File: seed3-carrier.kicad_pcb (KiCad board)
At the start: 2 copper layers, 113 x 61.6 mm, 48 parts, among them J1 AudioJack2_Switch, J2 AudioJack2, J3 5V_IN, J4 DISPLAY_UART, J5 SJ1-3535NG, J6 Seed3_PINS_RIGHT, J7 Seed3_PINS_LEFT, Q1 AO3401A, U1 TLV9062IDR, U2 TPA6111A2DR

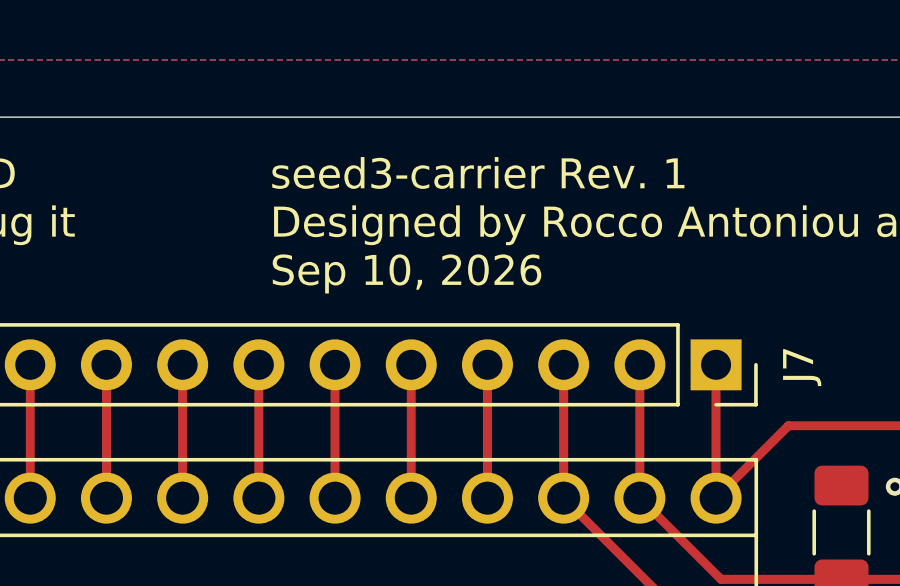
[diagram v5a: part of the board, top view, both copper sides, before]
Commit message: Simplify silkscreen revision date to Sep 2026
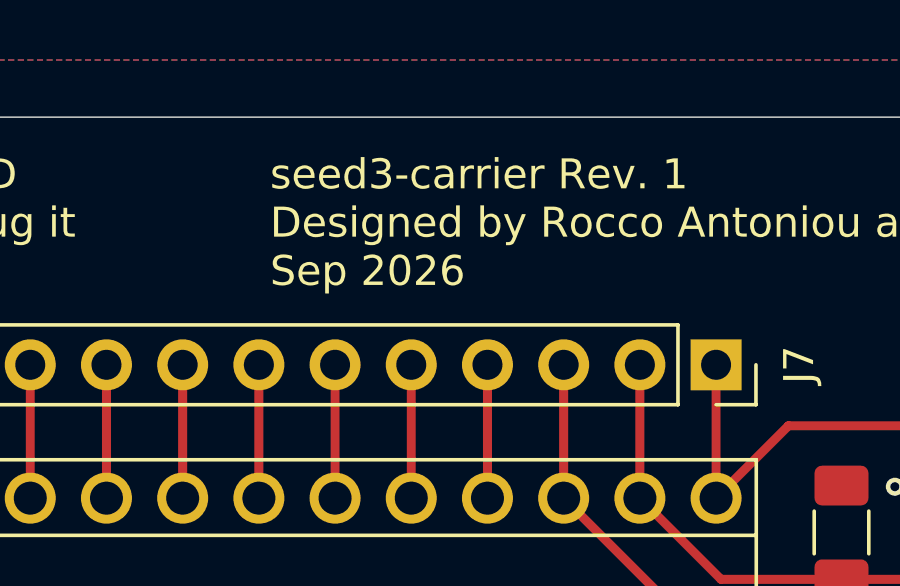
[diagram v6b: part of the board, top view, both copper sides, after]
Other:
- board text added: "seed3-carrier Rev. 1 Designed by Rocco Antoniou and Danny Diaz Reyes Sep 2026"
- board text removed: "seed3-carrier Rev. 1 Designed by Rocco Antoniou and Danny Diaz Reyes Sep 10, 2026"
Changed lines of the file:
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@@
 		)
 	)
-	(gr_text "seed3-carrier Rev. 1\nDesigned by Rocco Antoniou and Danny Diaz Reyes\nSep 10, 2026\n"
+	(gr_text "seed3-carrier Rev. 1\nDesigned by Rocco Antoniou and Danny Diaz Reyes\nSep 2026\n"
 		(at 86.106 45.72 0)
 		(layer "F.SilkS")

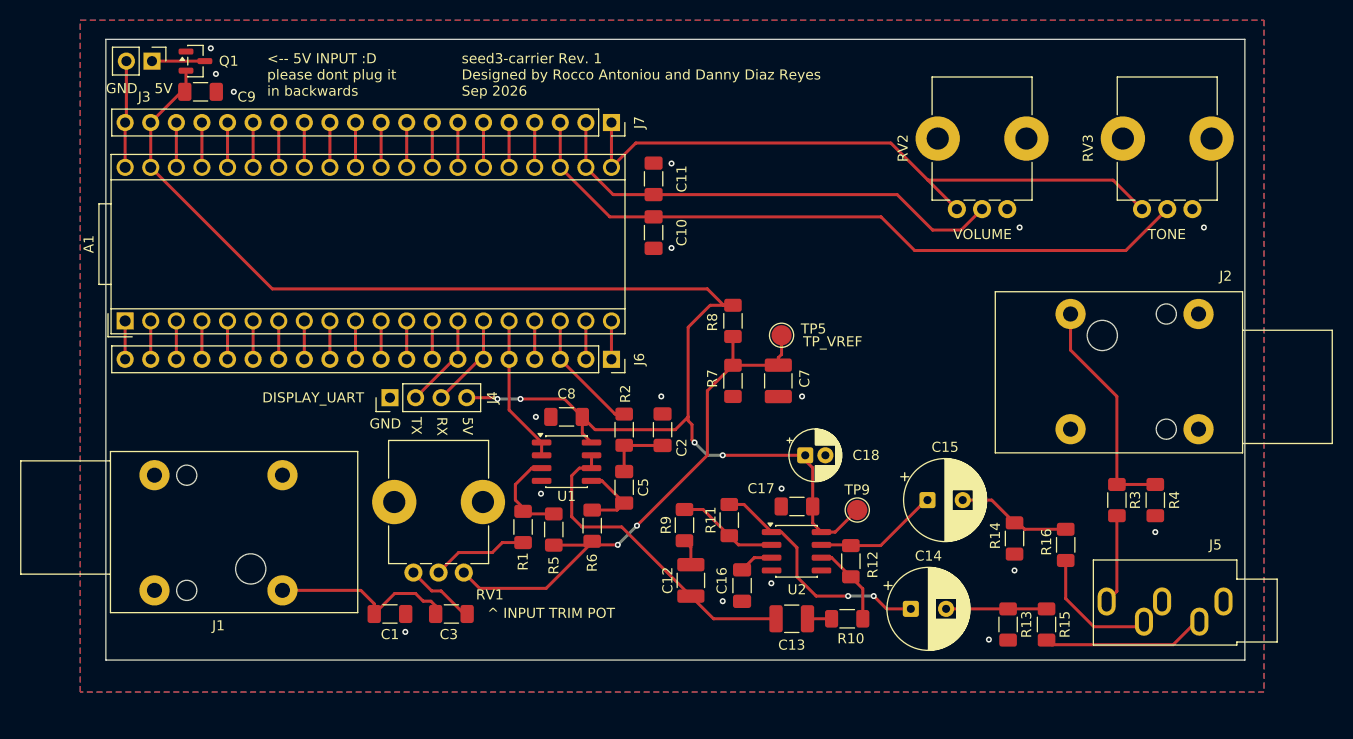
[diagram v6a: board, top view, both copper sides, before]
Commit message: Finalize potentiometer mounts and fabrication purchasing package
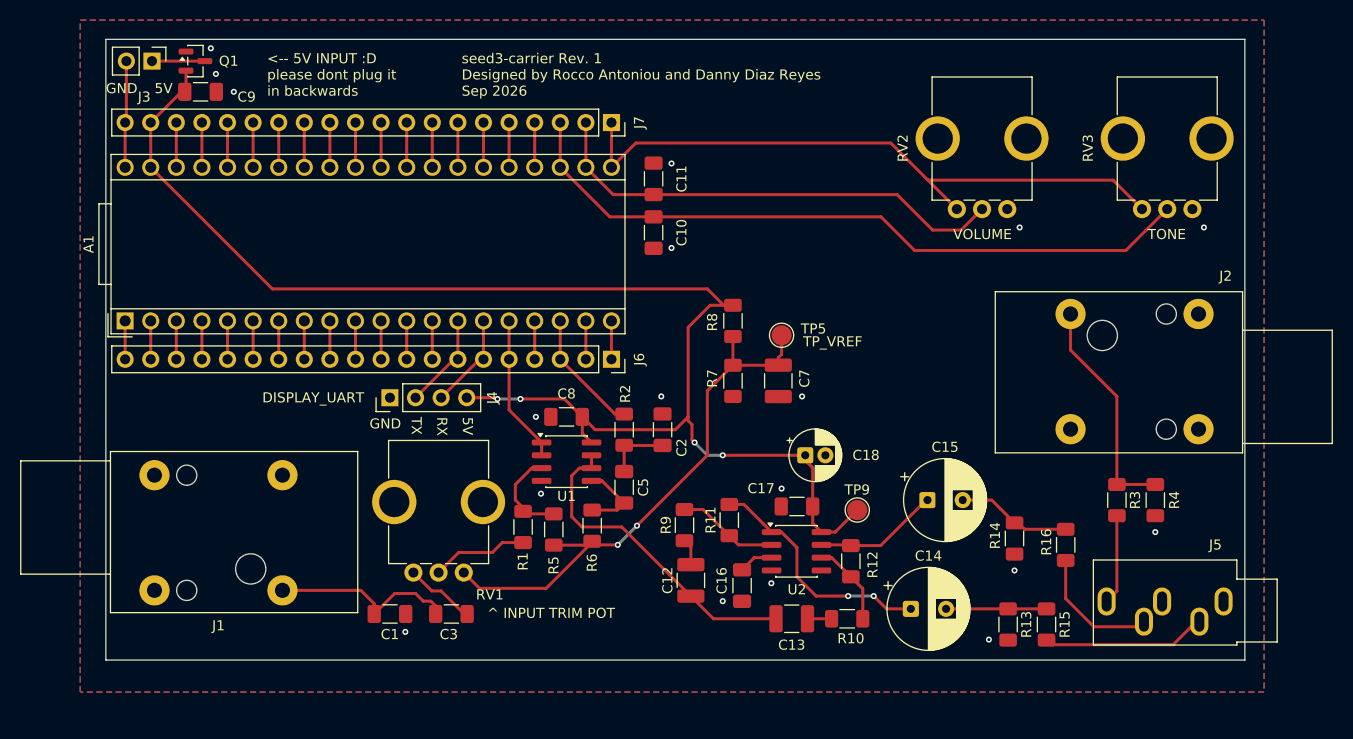
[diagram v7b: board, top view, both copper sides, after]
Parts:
- RV1, RV2, RV3: footprint Potentiometer_THT:Potentiometer_Bourns_PTV09A-1_Single_Vertical -> Seed3_Carrier:Potentiometer_Bourns_PTV09A-4_Single_Vertical_3mmMount
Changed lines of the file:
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@@
 		)
 	)
-	(footprint "Potentiometer_THT:Potentiometer_Bourns_PTV09A-1_Single_Vertical"
+	(footprint "Seed3_Carrier:Potentiometer_Bourns_PTV09A-4_Single_Vertical_3mmMount"
 		(layer "F.Cu")
 		(at 86.32 92.918 90)
@@
 			(at 7 -6.9 90)
 			(size 4.4 4.4)
-			(drill 2.2)
+			(drill 3)
 			(layers "*.Cu" "*.Mask")
 			(remove_unused_layers no)
@@
 			(at 7 1.9 90)
 			(size 4.4 4.4)
-			(drill 2.2)
+			(drill 3)
 			(layers "*.Cu" "*.Mask")
 			(remove_unused_layers no)
@@
 		)
 	)
-	(footprint "Potentiometer_THT:Potentiometer_Bourns_PTV09A-1_Single_Vertical"
+	(footprint "Seed3_Carrier:Potentiometer_Bourns_PTV09A-4_Single_Vertical_3mmMount"
 		(layer "F.Cu")
 		(at 158.625 56.85 90)
@@
 			(at 7 -6.9 90)
 			(size 4.4 4.4)
-			(drill 2.2)
+			(drill 3)
 			(layers "*.Cu" "*.Mask")
 			(remove_unused_layers no)
@@
 			(at 7 1.9 90)
 			(size 4.4 4.4)
-			(drill 2.2)
+			(drill 3)
 			(layers "*.Cu" "*.Mask")
 			(remove_unused_layers no)
@@
 		)
 	)
-	(footprint "Potentiometer_THT:Potentiometer_Bourns_PTV09A-1_Single_Vertical"
+	(footprint "Seed3_Carrier:Potentiometer_Bourns_PTV09A-4_Single_Vertical_3mmMount"
 		(layer "F.Cu")
 		(at 140.25 56.85 90)
@@
 			(at 7 -6.9 90)
 			(size 4.4 4.4)
-			(drill 2.2)
+			(drill 3)
 			(layers "*.Cu" "*.Mask")
 			(remove_unused_layers no)
@@
 			(at 7 1.9 90)
 			(size 4.4 4.4)
-			(drill 2.2)
+			(drill 3)
 			(layers "*.Cu" "*.Mask")
 			(remove_unused_layers no)

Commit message: Resize carrier board and finalize component placement
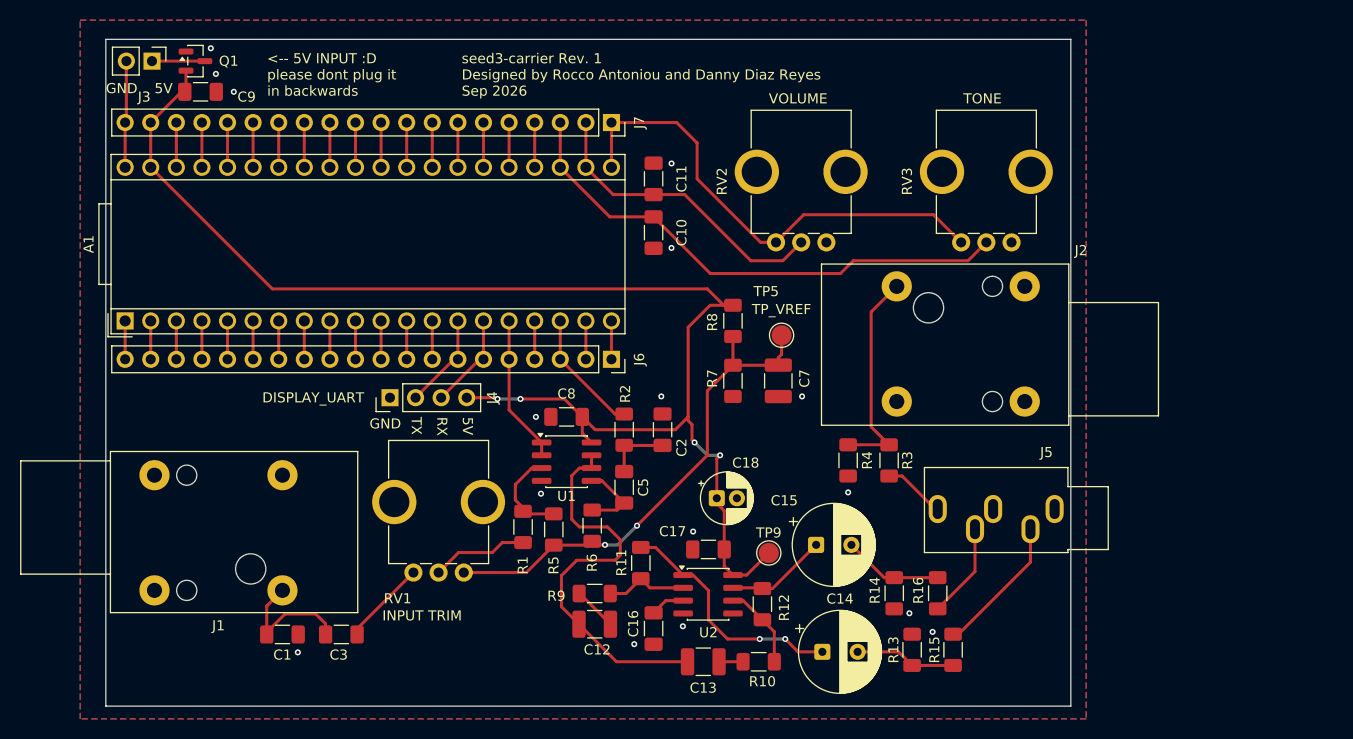
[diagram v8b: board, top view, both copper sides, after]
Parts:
- moved R4 30.7 mm to (124.5, 81.8)
- moved R3 22.9 mm to (128.5, 81.8)
- moved J5 19.1 mm to (144.9, 86.6)
- moved RV3 18.3 mm to (140.7, 60.2)
- moved RV2 18.3 mm to (122.3, 60.2)
- moved J2 17.5 mm to (129.3, 64.5)
- moved R16 13.6 mm to (133.3, 95.0)
- moved R14 13.1 mm to (129.0, 95.0)
- moved C15 11.9 mm to (121.3, 90.2)
- moved R9 11.2 mm to (99.3, 95.0), turned to 0 degrees
- moved C3 11.1 mm to (74.2, 99.1)
- moved C1 10.9 mm to (68.3, 99.1)
- moved C12 10.5 mm to (99.3, 98.0), turned to 0 degrees
- moved R13 9.85 mm to (130.8, 100.6), turned to 90 degrees
- moved C14 9.76 mm to (121.9, 100.8)
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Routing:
- net /TONE_POT: track 69.8 -> 52.4 mm
- net /VOLUME_POT: track 47.2 -> 30.4 mm
- net /3V3_A: track 64.9 -> 48.4 mm
- net /HP_SOURCE: track 32.1 -> 39.6 mm
- net Net-(C1-Pad1): track 18.9 -> 13.3 mm
- net /VREF: track 55.1 -> 49.7 mm
- net +5V: track 142.0 -> 138.0 mm
- net /HP_R: track 12.9 -> 9.44 mm
- net /LINE_SEND: track 8.94 -> 6.18 mm
- net /HP_L: track 16.3 -> 13.9 mm
- net Net-(U2-VOUT2): track 12.4 -> 10.1 mm
- net Net-(U2-IN1-): track 10.1 -> 8.21 mm
- net Net-(C12-Pad2): track 2.64 -> 4.38 mm
- net Net-(C15-Pad2): track 11.4 -> 9.91 mm
- net Net-(C3-Pad2): track 7.03 -> 8.46 mm
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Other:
- board size 113 x 61.6 mm -> 95.8 x 66.2 mm
- board text added: "INPUT TRIM"
- board text removed: "^ INPUT TRIM POT"
